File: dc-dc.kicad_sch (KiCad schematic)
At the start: 132 parts, among them SW3 CVS-02B, U30 NCP718ASN500T1G, U31 MPM54304GMN, U32 MPM54304GMN, U33 MAX16150AUT+T, U34 NCP451AFCT2G, U35 SN74LVC1G125DBVR, U36 LM3880, U37 MP8869S, U38 TPS7A20185PDQNR, U39 NCP51400MNTXG, U40 XC6230H001ER-G, U41 REF3012AIDBZT

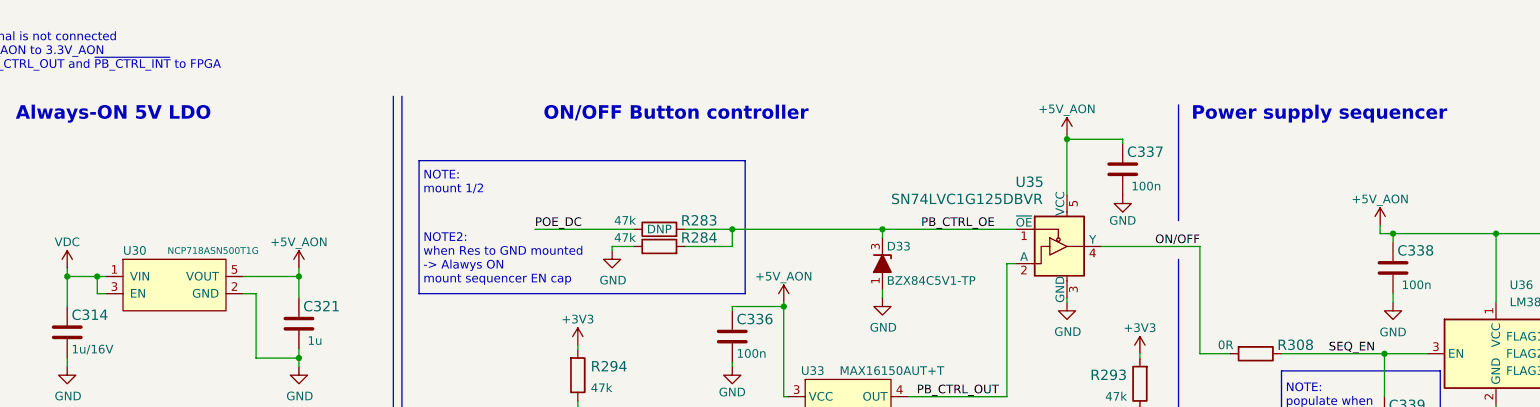
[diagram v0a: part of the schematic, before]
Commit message: Changed +5V_AON to +3V3_AON and LDO to 3.3V variant
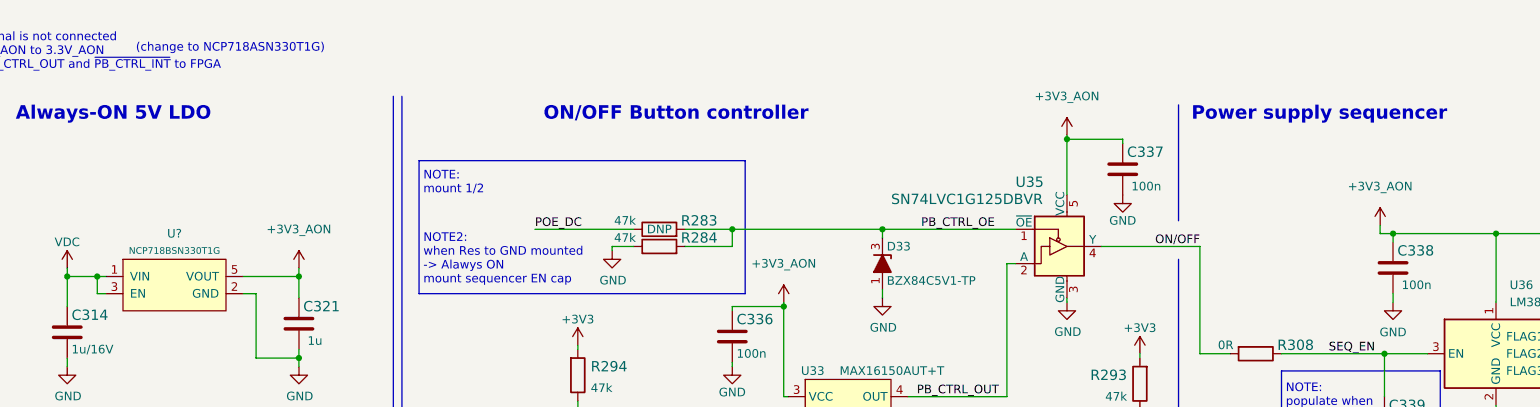
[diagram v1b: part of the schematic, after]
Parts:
- removed U30: NCP718ASN500T1G, antmicro-footprints:SOT-23-5, symbol antmicroPMICVoltageRegulatorsLinear:NCP718ASN500T1G
- added U?: NCP718BSN330T1G, antmicro-footprints:SOT-23-5, symbol antmicroPMICVoltageRegulatorsLinear:NCP718BSN330T1G
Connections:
- net GND: now also U?.2 (GND)
- net VDC: now also U?.1 (VIN), U?.3 (EN)
- net +5V_AON renamed +3V3_AON
- net +3V3_AON: now also U?.5 (VOUT)
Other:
- note added: "(change to NCP718ASN330T1G)"
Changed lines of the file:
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@@
     (effects (font (size 2 2) (thickness 0.254) bold) (justify left bottom))
   )
+  (text "(change to NCP718ASN330T1G)" (at 31.115 6.35 0)
+    (effects (font (size 1.27 1.27)) (justify left bottom))
+  )
   (text "Load switch" (at 106.68 276.225 0)
     (effects (font (size 1.27 1.27) (thickness 0.254) bold) (justify left bottom))
@@
     (pin "2")
   )
-  (symbol (lib_id "antmicroPower:+5V_AON") (at 168.91 18.415 0) (unit 1)
-    (in_bom yes) (on_board yes)
-    (property "Reference" "#PWR0359" (id 0) (at 168.91 22.225 0)
-      (effects (font (size 1.27 1.27)) hide)
-    )
-    (property "Value" "+5V_AON" (id 1) (at 168.91 14.605 0))
-    (property "Footprint" "" (id 2) (at 168.91 18.415 0)
-      (effects (font (size 1.27 1.27)) hide)
-    )
-    (property "Datasheet" "" (id 3) (at 168.91 18.415 0)
-      (effects (font (size 1.27 1.27)) hide)
-    )
-    (pin "1")
-  )
   (symbol (lib_id "antmicroCapacitors0402:C_100n_0402") (at 335.915 33.655 90) (unit 1)
     (in_bom yes) (on_board yes) (fields_autoplaced)
@@
     (pin "6")
   )
+  (symbol (lib_id "power:+3V3_AON") (at 127 43.18 0) (unit 1)
+    (in_bom yes) (on_board yes) (fields_autoplaced)
+    (property "Reference" "#PWR?" (id 0) (at 127 46.99 0)
+      (effects (font (size 1.27 1.27)) hide)
+    )
+    (property "Value" "+3V3_AON" (id 1) (at 127 37.465 0))
+    (property "Footprint" "" (id 2) (at 127 43.18 0)
+      (effects (font (size 1.27 1.27)) hide)
+    )
+    (property "Datasheet" "" (id 3) (at 127 43.18 0)
+      (effects (font (size 1.27 1.27)) hide)
+    )
+    (pin "1")
+  )
   (symbol (lib_id "power:VDC") (at 49.53 180.975 0) (unit 1)
     (in_bom yes) (on_board yes) (fields_autoplaced)
@@
     (pin "1")
   )
+  (symbol (lib_id "power:+3V3_AON") (at 55.245 38.1 0) (unit 1)
+    (in_bom yes) (on_board yes) (fields_autoplaced)
+    (property "Reference" "#PWR?" (id 0) (at 55.245 41.91 0)
+      (effects (font (size 1.27 1.27)) hide)
+    )
+    (property "Value" "+3V3_AON" (id 1) (at 55.245 32.385 0))
+    (property "Footprint" "" (id 2) (at 55.245 38.1 0)
+      (effects (font (size 1.27 1.27)) hide)
+    )
+    (property "Datasheet" "" (id 3) (at 55.245 38.1 0)
+      (effects (font (size 1.27 1.27)) hide)
+    )
+    (pin "1")
+  )
   (symbol (lib_id "antmicroCapacitors0603:C_22u_0603") (at 119.38 187.96 0) (unit 1)
     (in_bom yes) (on_board yes)
@@
     (pin "1")
   )
-  (symbol (lib_id "antmicroPower:+5V_AON") (at 127 43.18 0) (unit 1)
-    (in_bom yes) (on_board yes)
-    (property "Reference" "#PWR0349" (id 0) (at 127 46.99 0)
-      (effects (font (size 1.27 1.27)) hide)
-    )
-    (property "Value" "+5V_AON" (id 1) (at 127 39.37 0))
-    (property "Footprint" "" (id 2) (at 127 43.18 0)
-      (effects (font (size 1.27 1.27)) hide)
-    )
-    (property "Datasheet" "" (id 3) (at 127 43.18 0)
-      (effects (font (size 1.27 1.27)) hide)
-    )
-    (pin "1")
-  )
   (symbol (lib_id "antmicroCapacitors0402:C_100n_0402") (at 217.17 38.1 0) (unit 1)
     (in_bom yes) (on_board yes)
@@
     (pin "2")
   )
-  (symbol (lib_id "antmicroPower:+5V_AON") (at 215.265 31.75 0) (unit 1)
-    (in_bom yes) (on_board yes)
-    (property "Reference" "#PWR0372" (id 0) (at 215.265 35.56 0)
-      (effects (font (size 1.27 1.27)) hide)
-    )
-    (property "Value" "+5V_AON" (id 1) (at 215.265 27.94 0))
-    (property "Footprint" "" (id 2) (at 215.265 31.75 0)
-      (effects (font (size 1.27 1.27)) hide)
-    )
-    (property "Datasheet" "" (id 3) (at 215.265 31.75 0)
-      (effects (font (size 1.27 1.27)) hide)
-    )
-    (pin "1")
-  )
-  (symbol (lib_id "antmicroPMICVoltageRegulatorsLinear:NCP718ASN500T1G") (at 36.83 40.64 0) (unit 1)
-    (in_bom yes) (on_board yes)
-    (property "Reference" "U30" (id 0) (at 29.21 35.56 0)
-      (effects (font (size 1.27 1.27)) (justify left))
-    )
-    (property "Value" "NCP718ASN500T1G" (id 1) (at 42.545 35.56 0)
-      (effects (font (size 0.9906 0.9906)))
-    )
-    (property "Footprint" "antmicro-footprints:SOT-23-5" (id 2) (at 36.83 46.99 0)
-      (effects (font (size 1.27 1.27)) hide)
-    )
-    (property "Datasheet" "https://www.mouser.pl/datasheet/2/308/NCP718_D-1224359.pdf" (id 3) (at 39.37 31.75 0)
-      (effects (font (size 1.27 1.27)) hide)
-    )
-    (property "MPN" "NCP718ASN500T1G" (id 4) (at 33.02 33.02 0)
-      (effects (font (size 1.27 1.27)) hide)
-    )
-    (property "Manufacturer" "Onsemi" (id 5) (at 35.56 30.48 0)
-      (effects (font (size 1.27 1.27)) hide)
-    )
-    (pin "1")
-    (pin "2")
-    (pin "3")
-    (pin "5")
-  )
   (symbol (lib_id "antmicroResistors0402:R_330k_0402") (at 24.765 234.315 90) (unit 1)
     (in_bom yes) (on_board yes) (fields_autoplaced)
@@
     (pin "1")
   )
+  (symbol (lib_id "antmicroPMICVoltageRegulatorsLinear:NCP718BSN330T1G") (at 36.83 40.64 0) (unit 1)
+    (in_bom yes) (on_board yes) (fields_autoplaced)
+    (property "Reference" "U?" (id 0) (at 36.83 33.02 0))
+    (property "Value" "NCP718BSN330T1G" (id 1) (at 36.83 35.56 0)
+      (effects (font (size 0.9906 0.9906)))
+    )
+    (property "Footprint" "antmicro-footprints:SOT-23-5" (id 2) (at 36.83 46.99 0)
+      (effects (font (size 1.27 1.27)) hide)
+    )
+    (property "Datasheet" "https://www.mouser.pl/datasheet/2/308/NCP718_D-1224359.pdf" (id 3) (at 39.37 31.75 0)
+      (effects (font (size 1.27 1.27)) hide)
+    )
+    (property "MPN" "NCP718BSN330T1G" (id 4) (at 33.02 33.02 0)
+      (effects (font (size 1.27 1.27)) hide)
+    )
+    (property "Manufacturer" "Onsemi" (id 5) (at 35.56 30.48 0)
+      (effects (font (size 1.27 1.27)) hide)
+    )
+    (pin "1")
+    (pin "2")
+    (pin "3")
+    (pin "5")
+  )
   (symbol (lib_id "antmicroPower:+1V2_MGTAVTT") (at 384.175 107.95 0) (unit 1)
     (in_bom yes) (on_board yes) (fields_autoplaced)
@@
     (pin "2")
   )
+  (symbol (lib_id "power:+3V3_AON") (at 168.91 18.415 0) (unit 1)
+    (in_bom yes) (on_board yes) (fields_autoplaced)
+    (property "Reference" "#PWR?" (id 0) (at 168.91 22.225 0)
+      (effects (font (size 1.27 1.27)) hide)
+    )
+    (property "Value" "+3V3_AON" (id 1) (at 168.91 12.7 0))
+    (property "Footprint" "" (id 2) (at 168.91 18.415 0)
+      (effects (font (size 1.27 1.27)) hide)
+    )
+    (property "Datasheet" "" (id 3) (at 168.91 18.415 0)
+      (effects (font (size 1.27 1.27)) hide)
+    )
+    (pin "1")
+  )
   (symbol (lib_id "power:+1V35") (at 150.495 245.745 0) (unit 1)
     (in_bom yes) (on_board yes)
@@
     (pin "2")
   )
-  (symbol (lib_id "antmicroPower:+5V_AON") (at 55.245 38.1 0) (unit 1)
-    (in_bom yes) (on_board yes)
-    (property "Reference" "#PWR0335" (id 0) (at 55.245 41.91 0)
-      (effects (font (size 1.27 1.27)) hide)
-    )
-    (property "Value" "+5V_AON" (id 1) (at 55.245 34.29 0))
-    (property "Footprint" "" (id 2) (at 55.245 38.1 0)
-      (effects (font (size 1.27 1.27)) hide)
-    )
-    (property "Datasheet" "" (id 3) (at 55.245 38.1 0)
-      (effects (font (size 1.27 1.27)) hide)
-    )
-    (pin "1")
-  )
   (symbol (lib_id "data-center-dram-tester:GND") (at 141.605 42.545 0) (unit 1)
     (in_bom yes) (on_board yes)
@@
       (effects (font (size 1.27 1.27)) hide)
     )
+    (pin "1")
+  )
+  (symbol (lib_id "power:+3V3_AON") (at 215.265 31.75 0) (unit 1)
+    (in_bom yes) (on_board yes) (fields_autoplaced)
+    (property "Reference" "#PWR?" (id 0) (at 215.265 35.56 0)
+      (effects (font (size 1.27 1.27)) hide)
+    )
+    (property "Value" "+3V3_AON" (id 1) (at 215.265 26.035 0))
+    (property "Footprint" "" (id 2) (at 215.265 31.75 0)
+      (effects (font (size 1.27 1.27)) hide)
+    )
+    (property "Datasheet" "" (id 3) (at 215.265 31.75 0)
+      (effects (font (size 1.27 1.27)) hide)
+    )

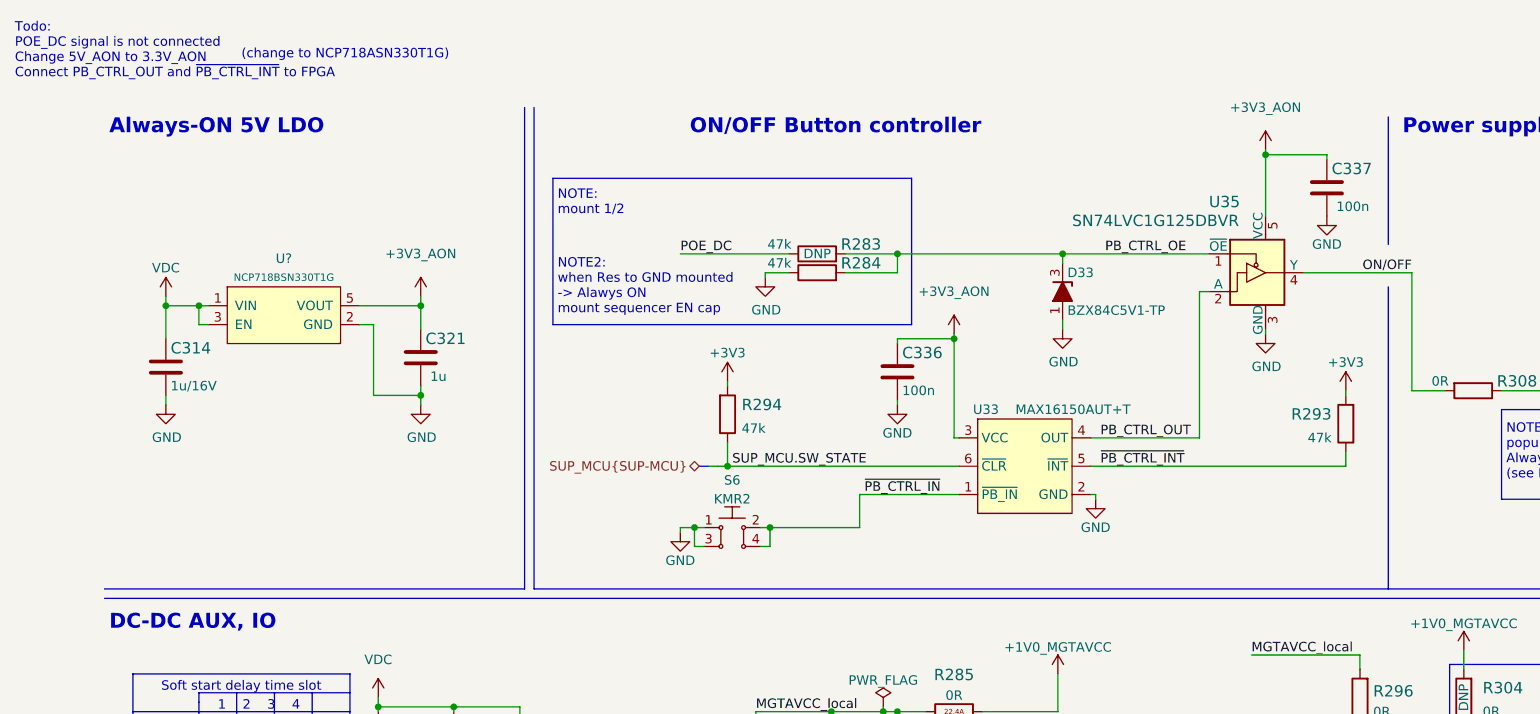
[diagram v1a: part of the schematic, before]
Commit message: Connected PB_CTRL_OUT and PB_CTRL_INT signals to FPGA
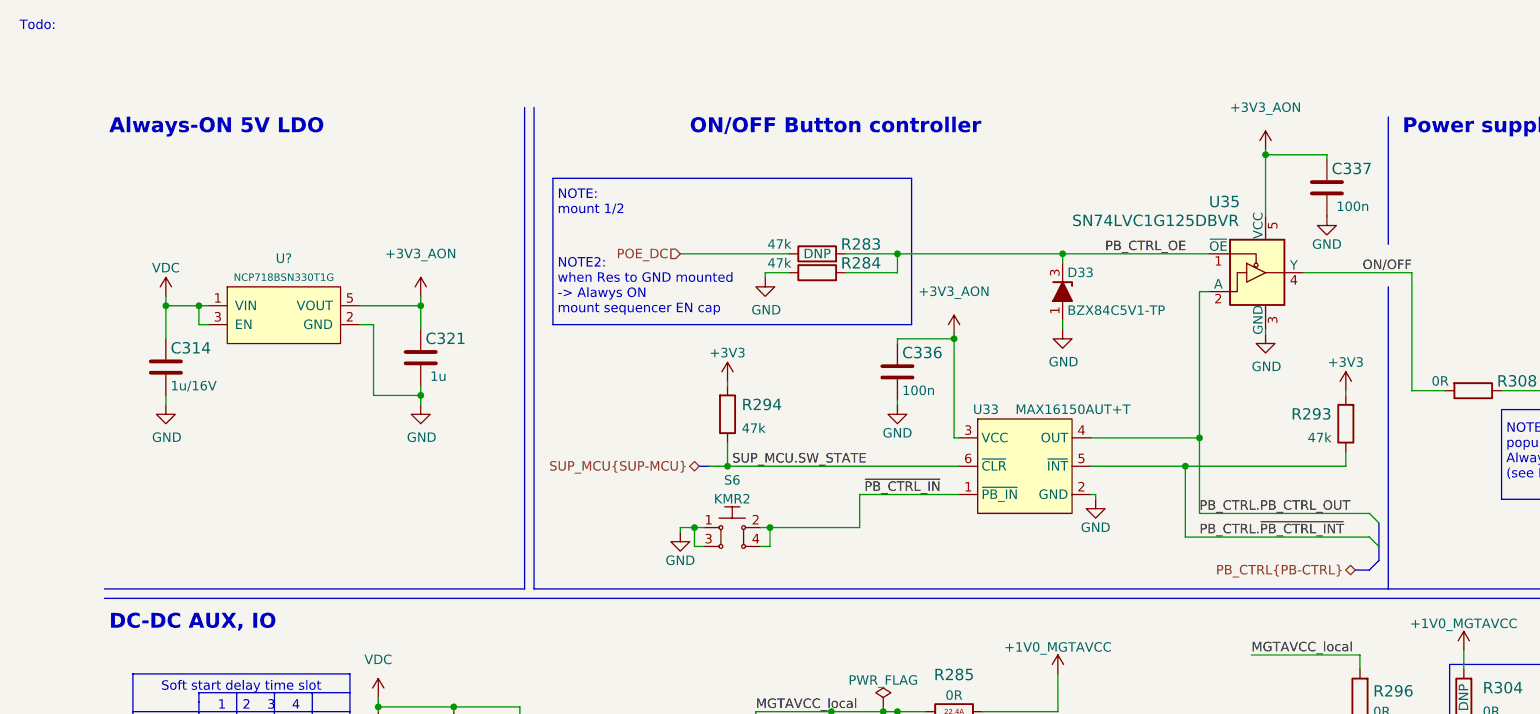
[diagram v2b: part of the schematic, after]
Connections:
- net PB_CTRL_OUT renamed PB_CTRL.PB_CTRL_OUT
- net ~{PB_CTRL_INT} renamed PB_CTRL.~{PB_CTRL_INT}
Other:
- note added: "Todo:"
- note removed: "(change to NCP718ASN330T1G)"
- note removed: "Todo: POE_DC signal is not connected Change 5V_AON to 3.3V_AON Connect PB_CTRL_OUT and ~{PB_CTRL_INT} to FPGA"
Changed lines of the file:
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@@
     (rev "0.0.99")
   )
+  (bus_alias "PB-CTRL" (members "PB_CTRL_OUT" "~{PB_CTRL_INT}"))
   (junction (at 362.585 45.085) (diameter 0) (color 0 0 0 0)
   )
@@
   (junction (at 370.205 45.085) (diameter 0) (color 0 0 0 0)
   )
+  (junction (at 158.115 60.96) (diameter 0) (color 0 0 0 0)
+  )
   (junction (at 350.52 121.92) (diameter 0) (color 0 0 0 0)
   )
@@
   )
   (junction (at 119.38 93.98) (diameter 0) (color 0 0 0 0)
+  )
+  (junction (at 160.02 57.15) (diameter 0) (color 0 0 0 0)
   )
   (junction (at 110.49 182.88) (diameter 0) (color 0 0 0 0)
@@
     (stroke (width 0) (type default) (color 0 0 0 0))
   )
+  (bus_entry (at 184.15 68.58) (size -1.27 -1.27)
+    (stroke (width 0) (type default) (color 0 0 0 0))
+  )
   (bus_entry (at 49.53 151.13) (size 1.27 -1.27)
     (stroke (width 0) (type default) (color 0 0 0 0))
@@
   )
   (bus_entry (at 49.53 153.67) (size 1.27 -1.27)
+    (stroke (width 0) (type default) (color 0 0 0 0))
+  )
+  (bus_entry (at 184.15 71.755) (size -1.27 -1.27)
     (stroke (width 0) (type default) (color 0 0 0 0))
   )
@@
     (stroke (width 0) (type default) (color 0 0 0 0))
   )
+  (wire (pts (xy 158.115 70.485) (xy 182.88 70.485))
+    (stroke (width 0) (type default) (color 0 0 0 0))
+  )
   (wire (pts (xy 24.765 229.235) (xy 24.765 229.87))
     (stroke (width 0) (type default) (color 0 0 0 0))
@@
     (stroke (width 0) (type default) (color 0 0 0 0))
   )
-  (wire (pts (xy 145.415 60.96) (xy 179.705 60.96))
+  (wire (pts (xy 145.415 60.96) (xy 158.115 60.96))
     (stroke (width 0) (type default) (color 0 0 0 0))
   )
@@
     (stroke (width 0) (type default) (color 0 0 0 0))
   )
+  (bus (pts (xy 184.15 71.755) (xy 184.15 73.66))
+    (stroke (width 0) (type default) (color 0 0 0 0))
+  )
   (wire (pts (xy 144.78 258.445) (xy 150.495 258.445))
     (stroke (width 0) (type default) (color 0 0 0 0))
@@
     (stroke (width 0) (type default) (color 0 0 0 0))
   )
+  (wire (pts (xy 160.02 67.31) (xy 160.02 57.15))
+    (stroke (width 0) (type default) (color 0 0 0 0))
+  )
   (wire (pts (xy 241.935 200.025) (xy 241.935 201.295))
     (stroke (width 0) (type default) (color 0 0 0 0))
@@
     (stroke (width 0) (type default) (color 0 0 0 0))
   )
+  (wire (pts (xy 158.115 60.96) (xy 158.115 70.485))
+    (stroke (width 0) (type default) (color 0 0 0 0))
+  )
   (wire (pts (xy 70.485 220.98) (xy 71.12 220.98))
     (stroke (width 0) (type default) (color 0 0 0 0))
@@
     (stroke (width 0) (type default) (color 0 0 0 0))
   )
+  (bus (pts (xy 184.15 68.58) (xy 184.15 71.755))
+    (stroke (width 0) (type default) (color 0 0 0 0))
+  )
   (wire (pts (xy 146.05 263.525) (xy 146.05 268.605))
     (stroke (width 0) (type default) (color 0 0 0 0))
@@
     (stroke (width 0) (type default) (color 0 0 0 0))
   )
+  (bus (pts (xy 184.15 73.66) (xy 182.88 74.93))
+    (stroke (width 0) (type default) (color 0 0 0 0))
+  )
   (wire (pts (xy 48.895 51.435) (xy 55.245 51.435))
     (stroke (width 0) (type default) (color 0 0 0 0))
@@
     (stroke (width 0) (type default) (color 0 0 0 0))
   )
+  (wire (pts (xy 158.115 60.96) (xy 179.705 60.96))
+    (stroke (width 0) (type default) (color 0 0 0 0))
+  )
   (wire (pts (xy 335.28 161.29) (xy 341.63 161.29))
     (stroke (width 0) (type default) (color 0 0 0 0))
@@
     (stroke (width 0) (type default) (color 0 0 0 0))
   )
+  (wire (pts (xy 160.02 67.31) (xy 182.88 67.31))
+    (stroke (width 0) (type default) (color 0 0 0 0))
+  )
   (polyline (pts (xy 43.18 187.96) (xy 43.18 180.34))
     (stroke (width 0) (type default) (color 0 0 0 0))
@@
   )
   (wire (pts (xy 387.985 64.135) (xy 387.985 65.405))
+    (stroke (width 0) (type default) (color 0 0 0 0))
+  )
+  (bus (pts (xy 182.88 74.93) (xy 180.975 74.93))
     (stroke (width 0) (type default) (color 0 0 0 0))
   )
@@
     (effects (font (size 1.27 1.27)) (justify left bottom))
   )
-  (text "Todo:\nPOE_DC signal is not connected\nChange 5V_AON to 3.3V_AON\nConnect PB_CTRL_OUT and ~{PB_CTRL_INT} to FPGA"
-    (at 0.635 8.89 0)
+  (text "Todo:" (at 1.27 2.54 0)
     (effects (font (size 1.27 1.27)) (justify left bottom))
   )
@@
     (effects (font (size 2 2) (thickness 0.254) bold) (justify left bottom))
   )
-  (text "(change to NCP718ASN330T1G)" (at 31.115 6.35 0)
-    (effects (font (size 1.27 1.27)) (justify left bottom))
-  )
   (text "Load switch" (at 106.68 276.225 0)
     (effects (font (size 1.27 1.27) (thickness 0.254) bold) (justify left bottom))
@@
     (effects (font (size 1.27 1.27)) (justify left bottom))
   )
-  (label "~{PB_CTRL_INT}" (at 146.685 60.96 0)
-    (effects (font (size 1.27 1.27)) (justify left bottom))
-  )
   (label "1V35_local" (at 231.14 227.965 0)
     (effects (font (size 1.27 1.27)) (justify left bottom))
@@
     (effects (font (size 1.27 1.27)) (justify left bottom))
   )
+  (label "PB_CTRL.~{PB_CTRL_INT}" (at 160.02 70.485 0)
+    (effects (font (size 1.27 1.27)) (justify left bottom))
+  )
   (label "SEQ_EN" (at 207.645 50.8 0)
     (effects (font (size 1.27 1.27)) (justify left bottom))
@@
     (effects (font (size 1.27 1.27)) (justify right bottom))
   )
-  (label "POE_DC" (at 90.17 32.385 0)
-    (effects (font (size 1.27 1.27)) (justify left bottom))
-  )
   (label "VDDR_VRI" (at 314.325 229.87 0)
     (effects (font (size 1.27 1.27)) (justify left bottom))
@@
     (effects (font (size 1.27 1.27)) (justify right bottom))
   )
-  (label "PB_CTRL_OUT" (at 146.685 57.15 0)
-    (effects (font (size 1.27 1.27)) (justify left bottom))
-  )
   (label "~{PB_CTRL_IN}" (at 114.935 64.77 0)
     (effects (font (size 1.27 1.27)) (justify left bottom))
@@
   )
   (label "FB2" (at 186.69 137.795 0)
+    (effects (font (size 1.27 1.27)) (justify left bottom))
+  )
+  (label "PB_CTRL.PB_CTRL_OUT" (at 160.02 67.31 0)
     (effects (font (size 1.27 1.27)) (justify left bottom))
   )
@@
     )
   )
+  (hierarchical_label "PB_CTRL{PB-CTRL}" (shape bidirectional) (at 180.975 74.93 180)
+    (effects (font (size 1.27 1.27)) (justify right))
+  )
   (hierarchical_label "SUP_MCU{SUP-MCU}" (shape bidirectional) (at 92.71 60.96 180)
     (effects (font (size 1.27 1.27)) (justify right))
   )
+  (hierarchical_label "POE_DC" (shape input) (at 90.17 32.385 180)
+    (effects (font (size 1.27 1.27)) (justify right))
+  )
